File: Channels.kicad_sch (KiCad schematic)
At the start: 22 parts, among them J7 Pullup_Sel, J8 Wiegand, J9 Scope, Q10 2N7002, Q11 2N7002, Q12 2N7002, Q9 BSS84

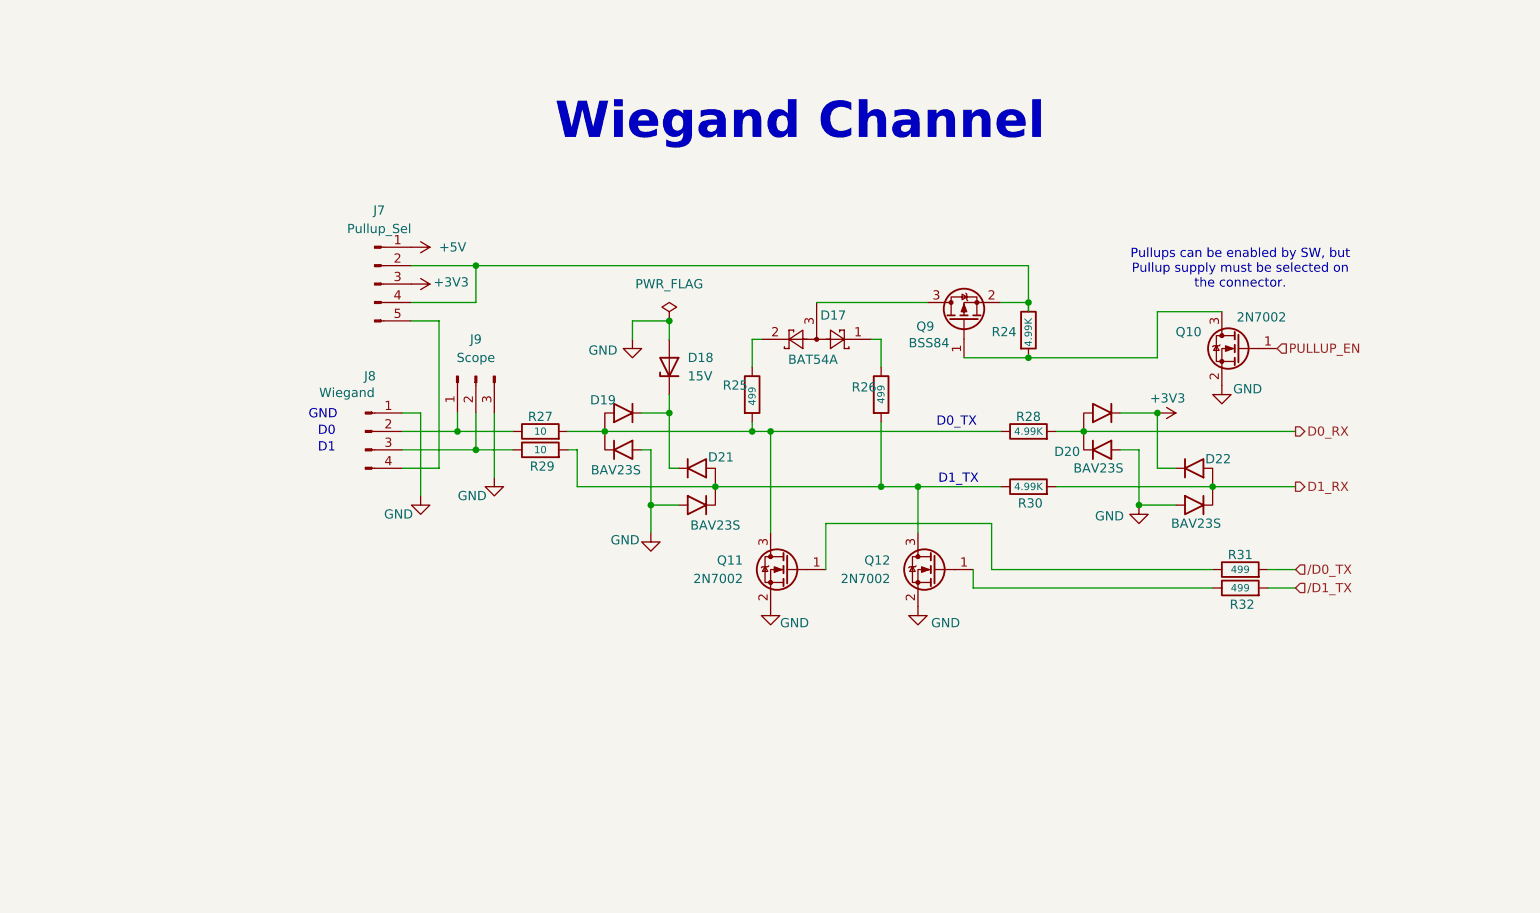
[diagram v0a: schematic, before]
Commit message: Mostly done.  Still need to do connections to LCD; waiting to get an actual LCD to verify connector location on PCB part.  May need to switch to 14 pin FFC, but hopefully not.
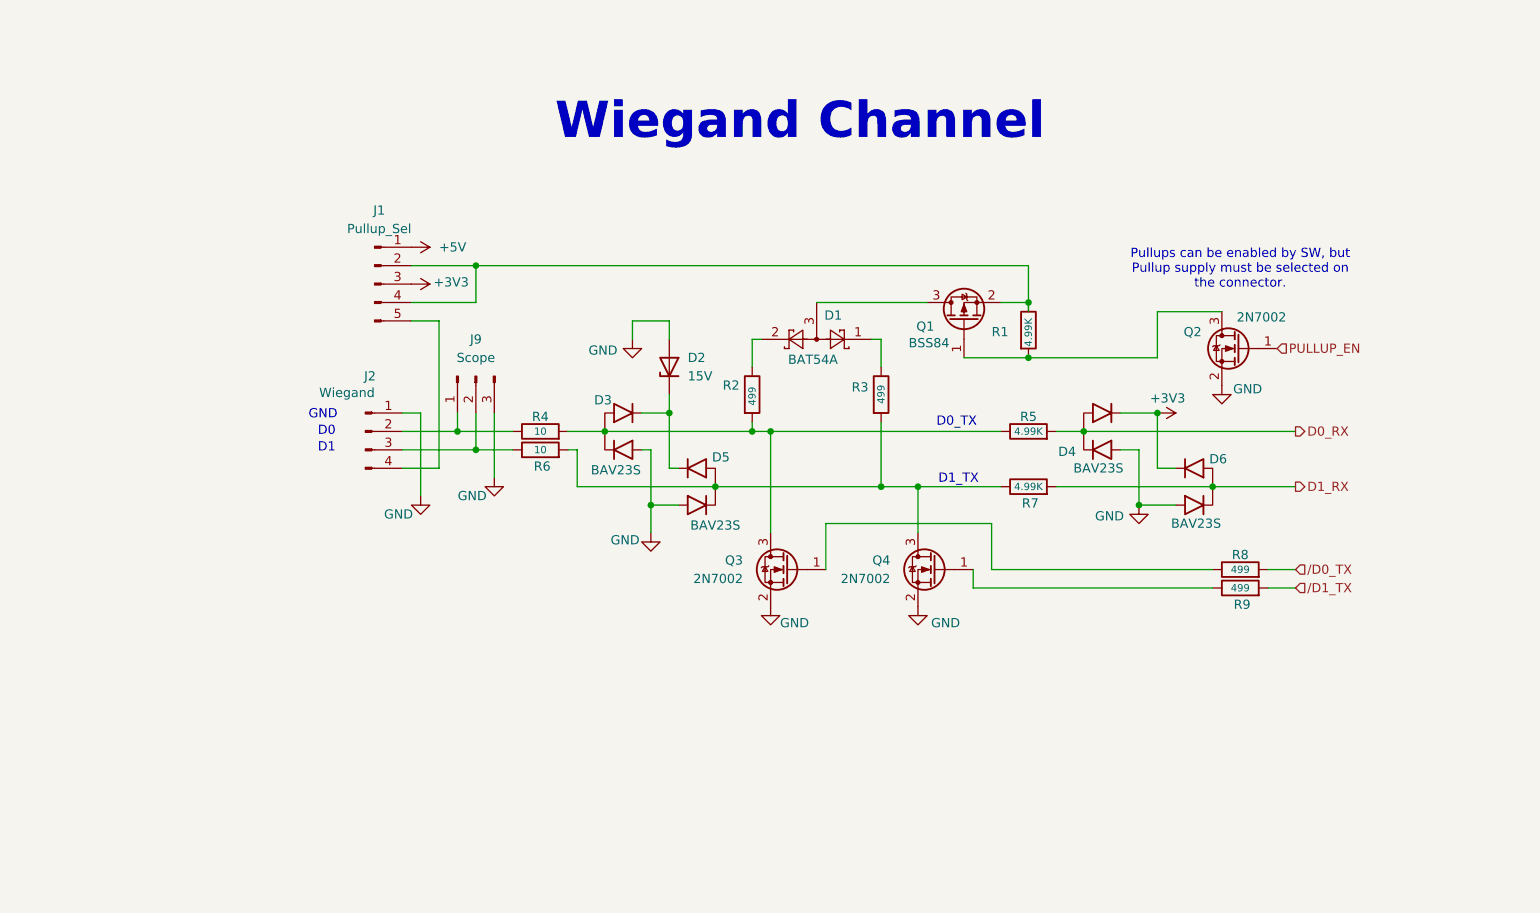
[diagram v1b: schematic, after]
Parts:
- renumbered D17 to D1, D18 to D2, D19 to D3, D20 to D4, D21 to D5, D22 to D6, J7 to J1, J8 to J2, Q9 to Q1, Q10 to Q2, Q11 to Q3, Q12 to Q4, R24 to R1, R25 to R2, R26 to R3, R27 to R4, R28 to R5, R29 to R6, R30 to R7, R31 to R8, R32 to R9
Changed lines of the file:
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@@
 	)
 	(junction
-		(at 119.38 64.77)
-		(diameter 0)
-		(color 0 0 0 0)
-	)
-	(junction
 		(at 176.53 80.01)
 		(diameter 0)
@@
 		(on_board yes)
 		(dnp no)
-		(property "Reference" "#PWR042"
+		(property "Reference" "#PWR07"
 			(at 184.15 96.52 0)
 			(effects
@@
 		(dnp no)
 		(fields_autoplaced yes)
-		(property "Reference" "J7"
+		(property "Reference" "J1"
 			(at 79.375 49.53 0)
 			(effects
@@
 		(on_board yes)
 		(dnp no)
-		(property "Reference" "R28"
+		(property "Reference" "R5"
 			(at 168.91 77.978 90)
 			(effects
@@
 		(on_board yes)
 		(dnp no)
-		(property "Reference" "D21"
+		(property "Reference" "D5"
 			(at 126.492 83.566 90)
 			(effects
@@
 		(on_board yes)
 		(dnp no)
-		(property "Reference" "#PWR043"
+		(property "Reference" "#PWR08"
 			(at 116.84 100.33 0)
 			(effects
@@
 		(on_board yes)
 		(dnp no)
-		(property "Reference" "D19"
+		(property "Reference" "D3"
 			(at 110.236 75.692 90)
 			(effects
@@
 		(on_board yes)
 		(dnp no)
-		(property "Reference" "D22"
+		(property "Reference" "D6"
 			(at 195.072 83.82 90)
 			(effects
@@
 		(on_board yes)
 		(dnp no)
-		(property "Reference" "R29"
+		(property "Reference" "R6"
 			(at 101.854 84.836 90)
 			(effects
@@
 		(on_board yes)
 		(dnp no)
-		(property "Reference" "#PWR045"
+		(property "Reference" "#PWR010"
 			(at 153.67 110.49 0)
 			(effects
@@
 		(on_board yes)
 		(dnp no)
-		(property "Reference" "D17"
+		(property "Reference" "D1"
 			(at 141.986 64.008 0)
 			(effects
@@
 		(on_board yes)
 		(dnp no)
-		(property "Reference" "R31"
+		(property "Reference" "R8"
 			(at 198.12 97.028 90)
 			(effects
@@
 		(on_board yes)
 		(dnp no)
-		(property "Reference" "R24"
+		(property "Reference" "R1"
 			(at 163.83 66.294 0)
 			(effects
@@
 		(on_board yes)
 		(dnp no)
-		(property "Reference" "Q10"
+		(property "Reference" "Q2"
 			(at 192.786 66.294 0)
 			(effects
@@
 		(on_board yes)
 		(dnp no)
-		(property "Reference" "Q9"
+		(property "Reference" "Q1"
 			(at 154.686 65.532 90)
 			(effects
@@
 		(dnp no)
 		(fields_autoplaced yes)
-		(property "Reference" "Q11"
+		(property "Reference" "Q3"
 			(at 129.54 97.7899 0)
 			(effects
@@
 		(dnp no)
 		(fields_autoplaced yes)
-		(property "Reference" "D18"
+		(property "Reference" "D2"
 			(at 121.92 69.8499 90)
 			(effects
@@
 		(on_board yes)
 		(dnp no)
-		(property "Reference" "R26"
+		(property "Reference" "R3"
 			(at 144.526 73.914 0)
 			(effects
@@
 		(dnp no)
 		(fields_autoplaced yes)
-		(property "Reference" "Q12"
+		(property "Reference" "Q4"
 			(at 149.86 97.7899 0)
 			(effects
@@
 		(on_board yes)
 		(dnp no)
-		(property "Reference" "#PWR044"
+		(property "Reference" "#PWR09"
 			(at 133.35 110.49 0)
 			(effects
@@
 		(on_board yes)
 		(dnp no)
-		(property "Reference" "#PWR039"
+		(property "Reference" "#PWR04"
 			(at 195.58 80.01 0)
 			(effects
@@
 		(on_board yes)
 		(dnp no)
-		(property "Reference" "D20"
+		(property "Reference" "D4"
 			(at 174.244 82.804 90)
 			(effects
@@
 	)
 	(symbol
-		(lib_id "power:PWR_FLAG")
-		(at 119.38 64.77 0)
-		(unit 1)
-		(exclude_from_sim no)
-		(in_bom yes)
-		(on_board yes)
-		(dnp no)
-		(fields_autoplaced yes)
-		(property "Reference" "#FLG05"
-			(at 119.38 62.865 0)
-			(effects
-				(font
-					(size 1.27 1.27)
-				)
-				(hide yes)
-			)
-		)
-		(property "Value" "PWR_FLAG"
-			(at 119.38 59.69 0)
-			(effects
-				(font
-					(size 1.27 1.27)
-				)
-			)
-		)
-		(property "Footprint" ""
-			(at 119.38 64.77 0)
-			(effects
-				(font
-					(size 1.27 1.27)
-				)
-				(hide yes)
-			)
-		)
-		(property "Datasheet" "~"
-			(at 119.38 64.77 0)
-			(effects
-				(font
-					(size 1.27 1.27)
-				)
-				(hide yes)
-			)
-		)
-		(property "Description" "Special symbol for telling ERC where power comes from"
-			(at 119.38 64.77 0)
-			(effects
-				(font
-					(size 1.27 1.27)
-				)
-				(hide yes)
-			)
-		)
-		(pin "1"
-		)
-		(instances
-			(project "WiegandTest"
-				(path "/0aeccc43-ea71-43b6-bfe2-e1aae0f9728d/86ccccb7-90dc-485a-a602-ad60cc7a093a"
-					(reference "#FLG01")
-					(unit 1)
-				)
-				(path "/0aeccc43-ea71-43b6-bfe2-e1aae0f9728d/9a734fd7-e5c3-43e5-a72d-1d275c512da8"
-					(reference "#FLG05")
-					(unit 1)
-				)
-				(path "/0aeccc43-ea71-43b6-bfe2-e1aae0f9728d/e04a91f8-dc5a-4f50-b3ea-99a97a1e543e"
-					(reference "#FLG04")
-					(unit 1)
-				)
-			)
-		)
-	)
-	(symbol
 		(lib_id "Connector:Conn_01x04_Pin")
 		(at 77.47 80.01 0)
@@
 		(on_board yes)
 		(dnp no)
-		(property "Reference" "J8"
+		(property "Reference" "J2"
 			(at 78.105 72.39 0)
 			(effects
@@
 		(on_board yes)
 		(dnp no)
-		(property "Reference" "R32"
+		(property "Reference" "R9"
 			(at 198.374 103.886 90)
 			(effects
@@
 		(on_board yes)
 		(dnp no)
-		(property "Reference" "#PWR038"
+		(property "Reference" "#PWR03"
 			(at 114.3 73.66 0)
 			(effects
@@
 		(on_board yes)
 		(dnp no)
-		(property "Reference" "#PWR037"
+		(property "Reference" "#PWR02"
 			(at 80.01 59.69 0)
 			(effects
@@
 		(dnp no)
 		(fields_autoplaced yes)
-		(property "Reference" "#PWR036"
+		(property "Reference" "#PWR01"
 			(at 80.01 54.61 0)
 			(effects
@@
 		(on_board yes)
 		(dnp no)
-		(property "Reference" "#PWR041"
+		(property "Reference" "#PWR06"
 			(at 85.09 95.25 0)
 			(effects
@@
 		(on_board yes)
 		(dnp no)
-		(property "Reference" "R27"
+		(property "Reference" "R4"
 			(at 101.6 77.978 90)
 			(effects
@@
 		(on_board yes)
 		(dnp no)
-		(property "Reference" "R30"
+		(property "Reference" "R7"
 			(at 169.164 89.916 90)
 			(effects
@@
 		(on_board yes)
 		(dnp no)
-		(property "Reference" "R25"
+		(property "Reference" "R2"
 			(at 126.746 73.66 0)
 			(effects
@@
 		(on_board yes)
 		(dnp no)
-		(property "Reference" "#PWR040"
+		(property "Reference" "#PWR05"
 			(at 182.88 77.47 0)
 			(effects

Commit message: OK, first basic layout complete - still need to do DRC and ERCs, get a good BOM going.
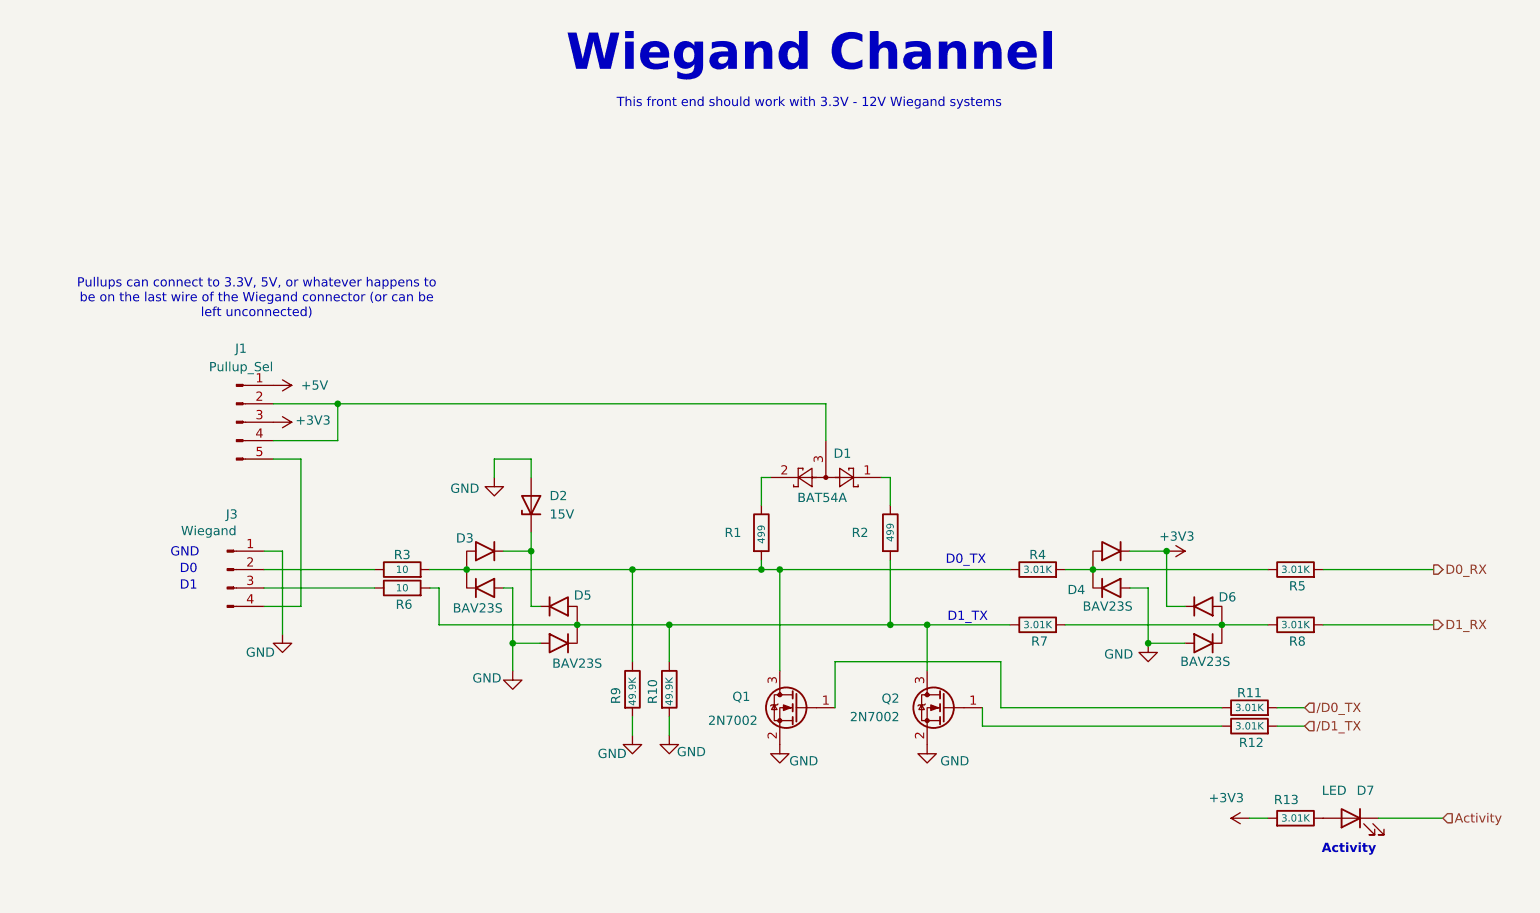
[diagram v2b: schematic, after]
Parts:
- removed J9: Scope, Connector_PinHeader_2.54mm:PinHeader_1x03_P2.54mm_Vertical, symbol Connector:Conn_01x03_Pin
- removed Q1: BSS84, Package_TO_SOT_SMD:SOT-23, symbol Transistor_FET:BSS84
- removed Q2: 2N7002, Package_TO_SOT_SMD:SOT-23, symbol Transistor_FET:2N7002
- removed R1: 4.99K, Resistor_SMD:R_0603_1608Metric_Pad0.98x0.95mm_HandSolder, symbol Device:R
- added D7: LED, LED_SMD:LED_0603_1608Metric_Pad1.05x0.95mm_HandSolder, symbol Device:LED
- added R10, R9: 49.9K, Resistor_SMD:R_0603_1608Metric_Pad0.98x0.95mm_HandSolder, symbol Device:R
- added R13, R5, R8: 3.01K, Resistor_SMD:R_0603_1608Metric_Pad0.98x0.95mm_HandSolder, symbol Device:R
- R11: renamed from R8; value 499 -> 3.01K
- R12: renamed from R9; value 499 -> 3.01K
- R4: renamed from R5; value 4.99K -> 3.01K
- R7: value 4.99K -> 3.01K
- renumbered J2 to J3, Q3 to Q1, Q4 to Q2, R2 to R1, R3 to R2, R4 to R3
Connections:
- net +3V3: now also R13.2
- net D0_RX: now also R5.2; no longer D4.3 (common), R4.2
- net D1_RX: now also R8.2; no longer D6.3 (common), R7.2
- net GND: now also R10.2, R9.2
- net at J1.2 (Pin_2), J1.4 (Pin_4): now also D1.3
- net at D3.3 (common), Q1.3 (D), R1.2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: now also R9.1
- net at D5.3 (common), Q2.3 (D), R2.2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: now also R10.1
- new net: D4.3 (common), R4.2, R5.1
- new net: D6.3 (common), R7.2, R8.1
- new net: D7.2 (A), R13.1
- new net Activity: D7.1 (K)
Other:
- note added: "Activity"
- note added: "Pullups can connect to 3.3V, 5V, or whatever happens to be on the last wire of the Wiegand connector (or can be left unconnected)"
- note added: "This front end should work with 3.3V - 12V Wiegand systems"
- note removed: "Pullups can be enabled by SW, but Pullup supply must be selected on the connector."
- moved on the sheet: D1, D2, D3, D4, D5, D6, J1, J3, Q1, Q2, R1, R11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

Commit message: BOM in schematic now completed via Digikey.  Board should be ready to build.
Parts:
- D1: MFG (none) -> Shenzhen Slkormicro Semicon; MPN (none) -> BAT54A
- D2: MFG (none) -> Onsemi
- D3, D4, D5, D6: MFG (none) -> Shenzhen Slkormicro Semicon
- D7: MFG (none) -> Lite-On; MPN (none) -> LTST-C191KGKT
- J1: MFG (none) -> Adam Tech; MPN (none) -> PH1RB-05-UA
- Q1, Q2: MFG (none) -> Onsemi; MPN (none) -> 2N7002
- R1, R2: MFG (none) -> YAGEO; MPN (none) -> RC0603FR-07499RL
- R10, R9: MFG (none) -> YAGEO; MPN (none) -> RC0603FR-1349K9L
- R11, R12, R13, R4, R5, R7, R8: MFG (none) -> YAGEO; MPN (none) -> RC0603FR-103K01L
- R3, R6: MFG (none) -> YAGEO; MPN (none) -> RC0603JR-1310RL

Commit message: Minor additions of text on schematics.
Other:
- note added: "Activity light turns on for 200 mSec if this channel receives a message"
- note added: "Green"
- note added: "Light pulldowns to anchor floating bus"
- note added: "Primary anti-static protection"
- note added: "Protection and 3.3V clamping if bus is higher than 3.3V"
- note added: "Pullup Voltage"
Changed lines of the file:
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@@
+		)
+	)
+	(text "Green"
+		(exclude_from_sim no)
+		(at 213.36 127.508 0)
+		(effects
+			(font
+				(size 1.27 1.27)
+			)
 		)
 	)
@@
 		)
 	)
+	(text "Protection and 3.3V clamping if\nbus is higher than 3.3V"
+		(exclude_from_sim no)
+		(at 181.356 90.678 0)
+		(effects
+			(font
+				(size 1.27 1.27)
+			)
+		)
+	)
+	(text "Activity light turns on for 200 mSec\nif this channel receives a message"
+		(exclude_from_sim no)
+		(at 211.582 142.24 0)
+		(effects
+			(font
+				(size 1.27 1.27)
+			)
+		)
+	)
 	(text "D0_TX"
 		(exclude_from_sim no)
@@
 	(text "D0"
 		(exclude_from_sim no)
-		(at 53.086 99.06 0)
+		(at 53.086 99.314 0)
+		(effects
+			(font
+				(size 1.27 1.27)
+			)
+		)
+	)
+	(text "Pullup Voltage"
+		(exclude_from_sim no)
+		(at 49.784 104.14 0)
+		(effects
+			(font
+				(size 1.27 1.27)
+			)
+		)
+	)
+	(text "Light pulldowns to \nanchor floating bus"
+		(exclude_from_sim no)
+		(at 114.554 129.286 0)
+		(effects
+			(font
+				(size 1.27 1.27)
+			)
+		)
+	)
+	(text "Primary anti-static \nprotection"
+		(exclude_from_sim no)
+		(at 84.328 111.252 0)
 		(effects
 			(font
@@
 	(text "D1"
 		(exclude_from_sim no)
-		(at 53.086 101.346 0)
+		(at 53.086 101.6 0)
 		(effects
 			(font
